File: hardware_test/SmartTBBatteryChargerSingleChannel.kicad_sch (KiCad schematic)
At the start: 151 parts, among them J1 XT60_MALE, J2 XT60_MALE, J3 XT60_MALE, J7 Conn_SWD, J8 Conn_01x02, Q1 BSC070N10NS5, Q2 BSC070N10NS5, Q3 BSC070N10NS5, U1 RY8411, U10 INA240A1PW, U2 RS3236, U3 RY8411, U4 STM32G474RBTx, U5 INA240A1PW, U6 UCC27517, U7 UCC27517, U8 INA240A1PW, U9 UCC27517, Y1 Crystal_GND24

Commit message: Update hardware_test/SmartTBBatteryChargerSingleChannel.kicad_sch
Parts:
- removed C40, C41, C50, C51, C52, C61: 100u, Capacitor_THT:CP_Radial_D6.3mm_P2.50mm, symbol Device:C_Polarized
- removed C42, C45, C46, C47, C49, C53, C56, C57, C58, C60: 100n, Capacitor_SMD:C_0603_1608Metric, symbol Device:C
- removed C43, C44, C48, C54, C55, C59: 10u, Capacitor_SMD:C_1206_3216Metric, symbol Device:C
- removed D5, D7: K34, Diode_SMD:D_SOD-123F, symbol Device:D_Schottky
- removed D6, D8: SB1045, Diode_SMD:D_PowerDI-5, symbol Device:D_Schottky
- removed F2, F3: 8A, Fuse:Fuse_1206_3216Metric, symbol Device:Fuse
- removed J2, J3: XT60_MALE, Connector_AMASS:AMASS_XT60-M_1x02_P7.20mm_Vertical, symbol Connector_Generic:Conn_01x02
- removed L4, L5: 47u, Inductor_SMD:L_Coilcraft_MSS1260-XXX, symbol Device:L
- removed Q2, Q3: BSC070N10NS5, Package_TO_SOT_SMD:TDSON-8-1, symbol Transistor_FET:BSC070N10NS5
- removed R11, R16: 1R, Resistor_SMD:R_0603_1608Metric, symbol Device:R
- removed R12, R17: 33R, Resistor_SMD:R_0603_1608Metric, symbol Device:R
- removed R13, R18: 10k, Resistor_SMD:R_0603_1608Metric, symbol Device:R
- removed R14, R19: 90k, Resistor_SMD:R_0603_1608Metric, symbol Device:R
- removed R15, R20: 4m, Resistor_SMD:R_Shunt_Vishay_WSK2512_6332Metric_T1.19mm, symbol Device:R_Shunt
- removed U10, U8: INA240A1PW, Package_SO:TSSOP-8_4.4x3mm_P0.65mm, symbol Amplifier_Current:INA240A1PW
- removed U7, U9: UCC27517, Package_TO_SOT_SMD:SOT-23-5, symbol 0_RM2024:UCC27517
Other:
- moved on the sheet: C1, C10, C100, C101, C102, C103, C11, C12, C13, C14, C15, C16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

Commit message: Test Hardware schematic done
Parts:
- removed C21: 100u 6.3V, Capacitor_SMD:C_1206_3216Metric, symbol Device:C
- removed D16: LED_RED, LED_SMD:LED_0603_1608Metric, symbol Device:LED
- removed R38: 240k, Resistor_SMD:R_0603_1608Metric, symbol Device:R
- added BZ1: Buzzer-9032, 0_RM2024:MLT-9032, symbol Device:Buzzer
- added C21: C_Polarized, Capacitor_THT:CP_Radial_D6.3mm_P2.50mm, symbol Device:C_Polarized
- added C40, C42, C48: 100u, Capacitor_THT:CP_Radial_D6.3mm_P2.50mm, symbol Device:C_Polarized
- added C41, C43, C44, C49, C50, C51, C52, C53: 100n, Capacitor_SMD:C_0603_1608Metric, symbol Device:C
- added C45, C46, C47: 10u, Capacitor_SMD:C_1206_3216Metric, symbol Device:C
- added C54, C55, C57: 10u, Capacitor_SMD:C_0603_1608Metric, symbol Device:C
- added C56: 20p, Capacitor_SMD:C_0603_1608Metric, symbol Device:C
- added D5: SB1045, Diode_SMD:D_PowerDI-5, symbol Device:D_Schottky
- added D6: K34, Diode_SMD:D_SOD-123F, symbol Device:D_Schottky
- added D7, D8: LED_WHITE, LED_SMD:LED_0603_1608Metric, symbol Device:LED
- added D9: DSS34, Diode_SMD:D_SMF, symbol Device:D_Schottky
- added F2: 8A, Fuse:Fuse_1206_3216Metric, symbol Device:Fuse
- added FB1: FerriteBead, Inductor_SMD:L_0603_1608Metric, symbol Device:FerriteBead
- added J2: XT60_MALE, Connector_AMASS:AMASS_XT60-M_1x02_P7.20mm_Vertical, symbol Connector_Generic:Conn_01x02
- added L4: 47u, Inductor_SMD:L_Coilcraft_MSS1260-XXX, symbol Device:L
- added Q2: BSC070N10NS5, Package_TO_SOT_SMD:TDSON-8-1, symbol Transistor_FET:BSC070N10NS5
- added Q3: AO3400A, Package_TO_SOT_SMD:SOT-23, symbol Transistor_FET:AO3400A
- added R11, R22: 33R, Resistor_SMD:R_0603_1608Metric, symbol Device:R
- added R12, R23: 4m, Resistor_SMD:R_Shunt_Vishay_WSK2512_6332Metric_T1.19mm, symbol Device:R_Shunt
- added R13: 1R, Resistor_SMD:R_0603_1608Metric, symbol Device:R
- added R14, R20, R24, R27: 10k, Resistor_SMD:R_0603_1608Metric, symbol Device:R
- added R15, R25: 90k, Resistor_SMD:R_0603_1608Metric, symbol Device:R
- added R16, R17, R26: 33r, Resistor_SMD:R_0603_1608Metric, symbol Device:R
- added R18: 1k, Resistor_SMD:R_0603_1608Metric, symbol Device:R
- added R19: 100k, Resistor_SMD:R_0603_1608Metric, symbol Device:R
- added R21: 2.2k, Resistor_SMD:R_0603_1608Metric, symbol Device:R
- added U7, U9: INA240A1PW, Package_SO:TSSOP-8_4.4x3mm_P0.65mm, symbol Amplifier_Current:INA240A1PW
- added U8: UCC27517, Package_TO_SOT_SMD:SOT-23-5, symbol 0_RM2024:UCC27517
- J8: footprint Connector_AMASS:AMASS_XT60PW-M_1x02_P7.20mm_Horizontal -> Connector_AMASS:AMASS_XT30U-M_1x02_P5.0mm_Vertical
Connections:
- net +10V: now also C49.1, R19.1, U8.1 (V_{DD})
- net +3.3V: now also C41.1, C51.1, C57.2, R21.1, U7.5 (V+), U9.5 (V+); no longer U5.6 (REF2)
- net +5V: now also C21.1, FB1.1, R20.1
- net DRV_CH1: now also R16.1
- net GND: now also D17.1 (K), U4.15 (VSS), U4.27 (VSSA), U4.31 (VSS), U4.47 (VSS), U4.63 (VSS), C21.2, C40.2, C41.2, C42.2, C43.2, C44.1, C45.2, C46.2, C49.2, C50.1, C51.2, C52.1, C53.1, C54.1, C55.1, C57.1, D7.1 (K), D8.1 (K), Q2.1 (S), Q2.2 (S), Q2.3 (S), Q3.2 (S), R14.1, R18.1, R24.1, R27.1, U7.1 (GND), U7.4 (GND), U7.7 (REF1), U8.2 (GND), U8.4 (IN-), U9.1 (GND), U9.4 (GND), U9.7 (REF1)
- net ISENSE_CH1: now also U4.8 (PC0)
- net VPP: now also C40.1, C42.1, C43.1, C45.1, C46.1, C47.1, C48.1, D5.1 (K), R12.1, R23.1, R25.2; no longer F8.1
- net VSENSE_CH1: now also U4.21 (PA7)
- net +2V5: now reaches C90.2, C91.2, U4.28 (VREF+)
- net +2V5: now also U5.6 (REF2), U7.6 (REF2), U9.6 (REF2)
- net VSENSE_INPUT: now reaches U4.35 (PB13)
- net VSENSE_INPUT: now also C53.2, R24.2, R25.1
- net at U4.42 (PA8): now also R16.2
- net at U4.44 (PA10): now also R17.2
- net RGB_DATA: now reaches U4.45 (PA11)
- net RGB_DATA: now also D18.3 (DIN)
- net BUZZER: now reaches U4.54 (PC12)
- net BUZZER: now also R26.1, R27.2
- net at U4.61 (PB8): now also R18.2
- net ISENSE_CH2: now reaches U4.9 (PC1)
- net ISENSE_CH2: now also C44.2, R11.1
- net at D17.2 (A): now also R19.2
- net BOOT0 renamed VSENSE_CH2
- net VSENSE_CH2: now also C50.2, R14.2, R15.1
- new net: F2.1, J2.1 (Pin_1)
- new net: J2.2 (Pin_2), R12.4
- new net: R11.2, U7.8
- new net: BZ1.2 (+), C54.2, C55.2, C56.2, D9.1 (K), FB1.2
- new net: BZ1.1 (-), C56.1, D9.2 (A), Q3.3 (D)
- new net: D6.1 (K), R13.1, U8.5 (OUT)
- new net: D7.2 (A), R20.2
- new net: D6.2 (A), Q2.4 (G), R13.2
- new net: C47.2, C48.2, F2.2, L4.2, R15.2
- new net: D5.2 (A), L4.1, Q2.5 (D)
- new net: R23.2, U9.3 (-)
- new net: R23.3, U9.2 (+)
- new net: F8.1, R23.4
- new net: Q3.1 (G), R26.2
- new net: R12.3, U7.2 (+)
- new net: R12.2, U7.3 (-)
- new net: D8.2 (A), R21.2
- new net: R22.2, U9.8
- new net DRV_CH2: R17.1, U8.3 (IN+)
- new net ISENSE_INPUT: C52.2, R22.1
- no-connect marks 0 -> 37
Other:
- moved on the sheet: C1, C10, C11, C12, C13, C14, C15, C16, C17, C18, C19, C2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

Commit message: Progress on hardware_test PCB
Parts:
- removed C24: 100n, Capacitor_SMD:C_0603_1608Metric, symbol Device:C
- removed Y1: Crystal_GND24, Crystal:Crystal_SMD_3225-4Pin_3.2x2.5mm, symbol Device:Crystal_GND24
- added Y3: CSTCE8M, Crystal:Resonator_SMD_Murata_CSTxExxV-3Pin_3.0x1.1mm_HandSoldering, symbol Device:Resonator
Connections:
- net GND: now also Y3.2
- net at U4.5 (PF0): now also Y3.1
- net at U4.6 (PF1): now also Y3.3
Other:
- moved on the sheet: C23

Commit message: just more wiring...
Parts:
- BZ1: footprint 0_RM2024:MLT-9032 -> LinkedLibrary:MLT-9032
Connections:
- net ISENSE_INPUT: now also U4.10 (PC2)
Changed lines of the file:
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@@
 	)
 	(no_connect
-		(at 57.15 81.28)
-	)
-	(no_connect
 		(at 92.71 91.44)
 	)
@@
 	)
 	(no_connect
+		(at 365.76 193.04)
+	)
+	(no_connect
 		(at 92.71 101.6)
 	)
@@
 		)
 	)
+	(global_label "ISENSE_INPUT"
+		(shape input)
+		(at 57.15 81.28 180)
+		(fields_autoplaced yes)
+		(effects
+			(font
+				(size 1.27 1.27)
+			)
+			(justify right)
+		)
+		(property "Intersheetrefs" "${INTERSHEET_REFS}"
+			(at 41.0415 81.28 0)
+			(effects
+				(font
+					(size 1.27 1.27)
+				)
+				(justify right)
+				(hide yes)
+			)
+		)
+	)
 	(symbol
 		(lib_id "Device:C")
@@
 			)
 		)
-		(property "Footprint" "0_RM2024:MLT-9032"
+		(property "Footprint" "LinkedLibrary:MLT-9032"
 			(at 211.455 252.73 90)
 			(effects

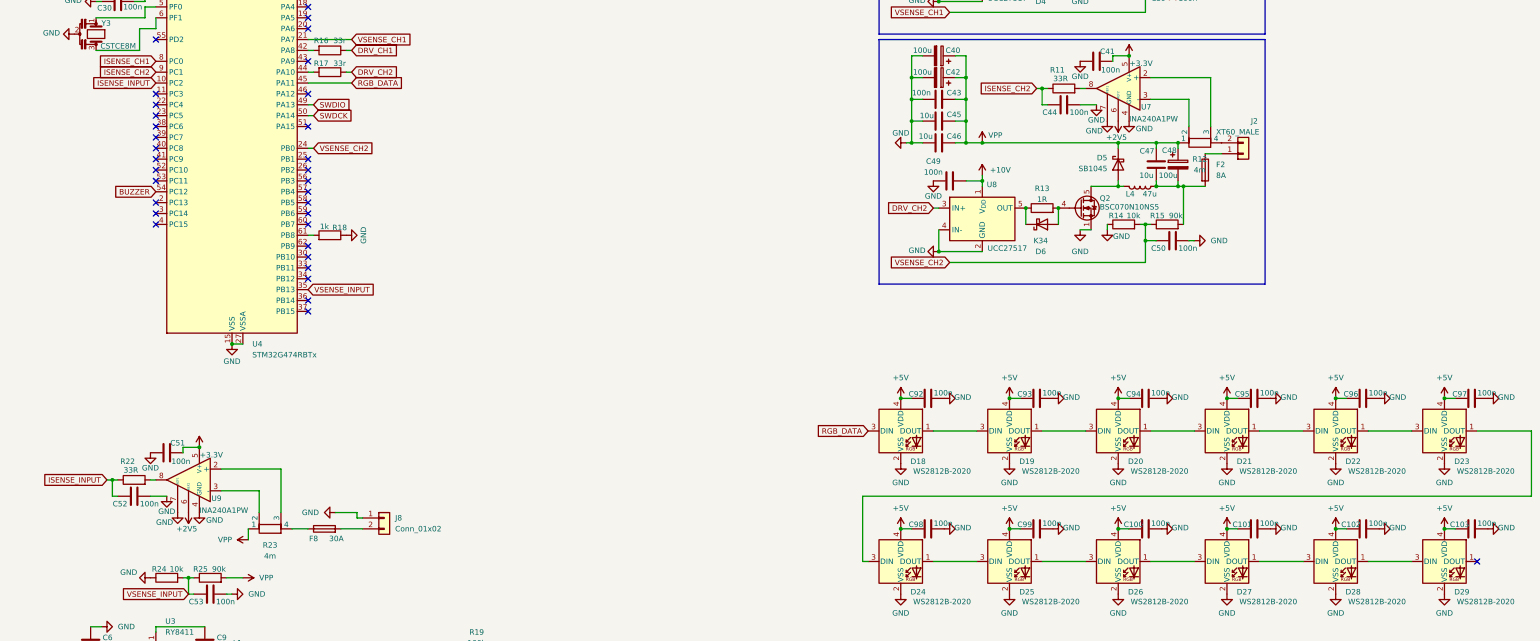
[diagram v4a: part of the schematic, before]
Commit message: Revert "just more wiring..."
This reverts commit 3ec1996944e63c1d6ae5bd01b13986183c75ca17.
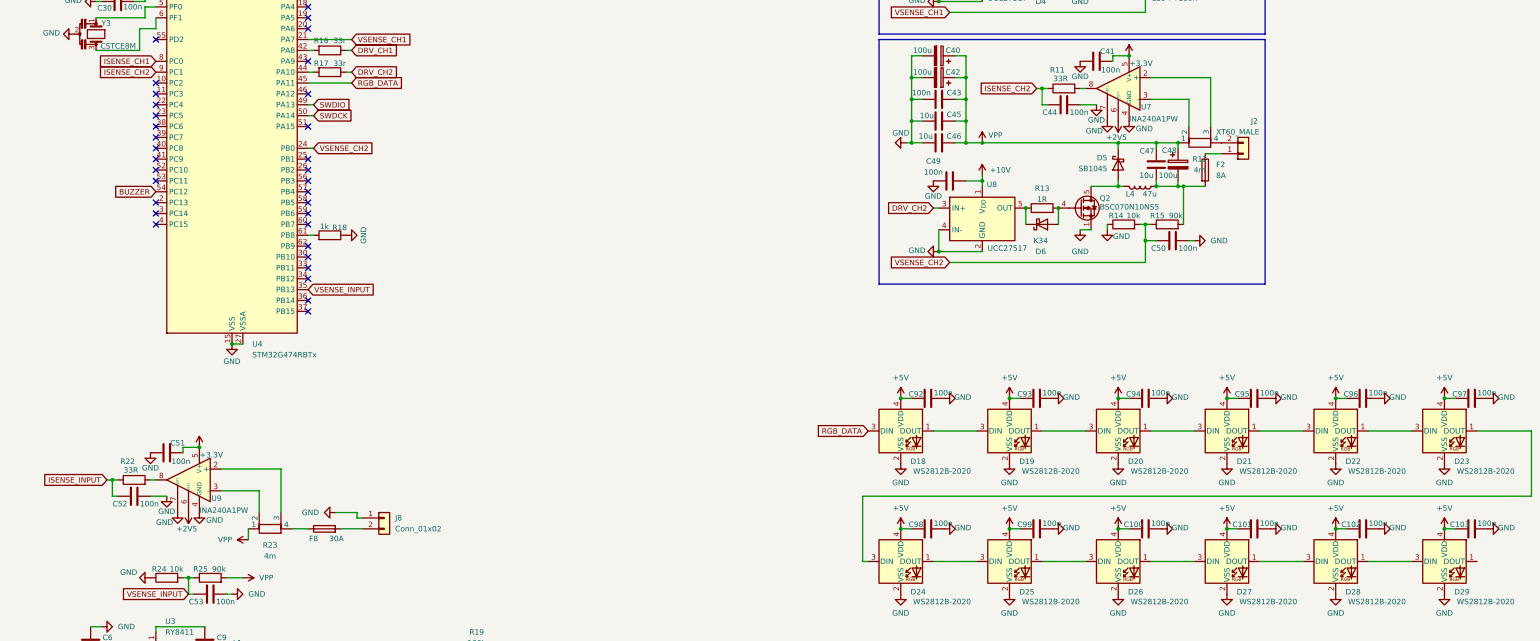
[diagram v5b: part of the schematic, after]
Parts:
- BZ1: footprint LinkedLibrary:MLT-9032 -> 0_RM2024:MLT-9032
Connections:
- net ISENSE_INPUT: no longer U4.10 (PC2)
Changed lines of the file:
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@@
 	)
 	(no_connect
+		(at 57.15 81.28)
+	)
+	(no_connect
 		(at 92.71 91.44)
 	)
@@
 	)
 	(no_connect
-		(at 365.76 193.04)
-	)
-	(no_connect
 		(at 92.71 101.6)
 	)
@@
 		)
 	)
-	(global_label "ISENSE_INPUT"
-		(shape input)
-		(at 57.15 81.28 180)
-		(fields_autoplaced yes)
-		(effects
-			(font
-				(size 1.27 1.27)
-			)
-			(justify right)
-		)
-		(property "Intersheetrefs" "${INTERSHEET_REFS}"
-			(at 41.0415 81.28 0)
-			(effects
-				(font
-					(size 1.27 1.27)
-				)
-				(justify right)
-				(hide yes)
-			)
-		)
-	)
 	(symbol
 		(lib_id "Device:C")
@@
 			)
 		)
-		(property "Footprint" "LinkedLibrary:MLT-9032"
+		(property "Footprint" "0_RM2024:MLT-9032"
 			(at 211.455 252.73 90)
 			(effects
